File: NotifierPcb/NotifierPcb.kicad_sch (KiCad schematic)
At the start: 29 parts, among them IC1 CD4067BEE4, IC2 ESP32-WROOM-32E__8MB_, J1 RC_433_MHZ_RF, J2 UART_Conn, J3 Power_Conn, U1 HT75xx-1-SOT89

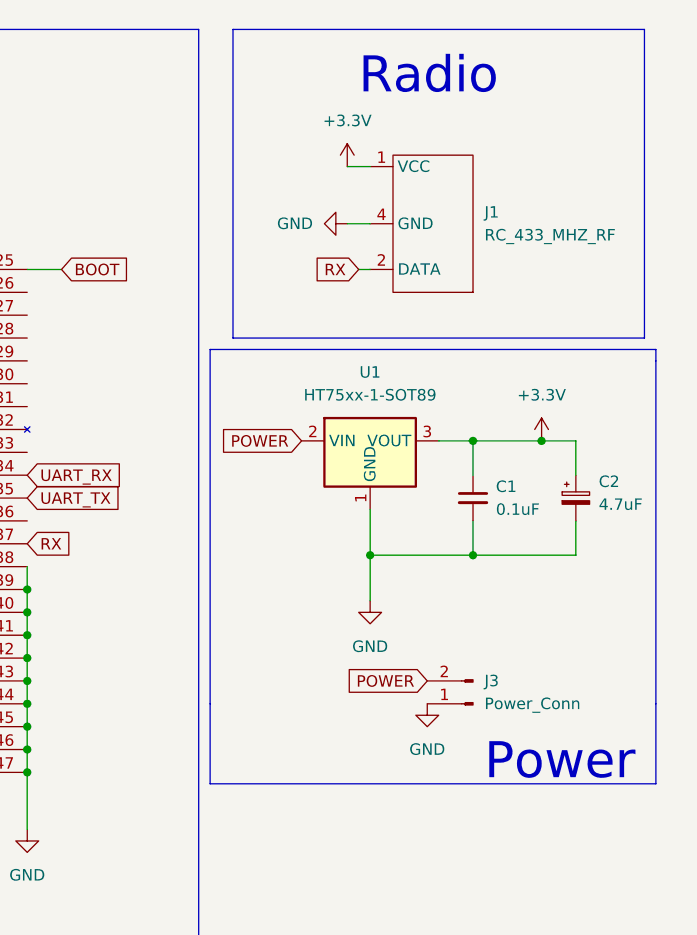
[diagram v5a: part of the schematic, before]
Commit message: power rf receiver with 5V
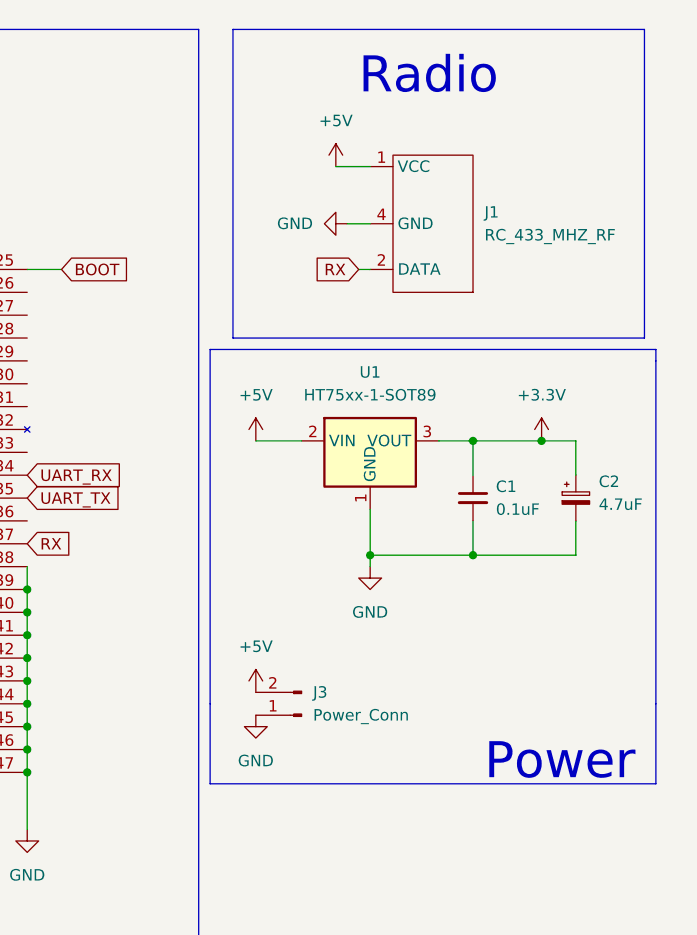
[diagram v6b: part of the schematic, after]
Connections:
- net +3.3V: no longer J1.1 (VCC)
- net POWER renamed +5V
- net +5V: now also J1.1 (VCC)
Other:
- moved on the sheet: J3
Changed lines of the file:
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@@
+    (stroke (width 0) (type default) (color 0 0 0 0))
+  )
+  (wire (pts (xy 238.76 64.77) (xy 243.84 64.77))
     (stroke (width 0) (type default) (color 0 0 0 0))
   )
@@
     (stroke (width 0) (type default) (color 0 0 0 0))
   )
-  (wire (pts (xy 248.92 34.29) (xy 251.46 34.29))
+  (wire (pts (xy 247.65 34.29) (xy 251.46 34.29))
     (stroke (width 0) (type default) (color 0 0 0 0))
   )
@@
     (stroke (width 0) (type default) (color 0 0 0 0))
   )
-  (wire (pts (xy 251.46 77.47) (xy 251.46 82.55))
+  (wire (pts (xy 251.46 77.47) (xy 251.46 78.74))
     (stroke (width 0) (type default) (color 0 0 0 0))
   )
@@
     )
   )
-  (global_label "POWER" (shape input) (at 257.81 91.44 180) (fields_autoplaced)
-    (effects (font (size 1.27 1.27)) (justify right))
-    (property "Intersheet References" "${INTERSHEET_REFS}" (id 0) (at 248.9259 91.3606 0)
-      (effects (font (size 1.27 1.27)) (justify right) hide)
-    )
-  )
   (global_label "BIT3" (shape input) (at 175.26 63.5 180) (fields_autoplaced)
     (effects (font (size 1.27 1.27)) (justify right))
@@
     (effects (font (size 1.27 1.27)) (justify right))
     (property "Intersheet References" "${INTERSHEET_REFS}" (id 0) (at 159.6631 138.5094 0)
-      (effects (font (size 1.27 1.27)) (justify right) hide)
-    )
-  )
-  (global_label "POWER" (shape input) (at 243.84 64.77 180) (fields_autoplaced)
-    (effects (font (size 1.27 1.27)) (justify right))
-    (property "Intersheet References" "${INTERSHEET_REFS}" (id 0) (at 234.9559 64.6906 0)
       (effects (font (size 1.27 1.27)) (justify right) hide)
     )
@@
     (pin "2")
     (pin "3")
+  )
+  (symbol (lib_id "power:+5V") (at 238.76 92.71 0) (unit 1)
+    (in_bom yes) (on_board yes) (fields_autoplaced)
+    (property "Reference" "#PWR?" (id 0) (at 238.76 96.52 0)
+      (effects (font (size 1.27 1.27)) hide)
+    )
+    (property "Value" "+5V" (id 1) (at 238.76 87.63 0))
+    (property "Footprint" "" (id 2) (at 238.76 92.71 0)
+      (effects (font (size 1.27 1.27)) hide)
+    )
+    (property "Datasheet" "" (id 3) (at 238.76 92.71 0)
+      (effects (font (size 1.27 1.27)) hide)
+    )
+    (pin "1")
   )
   (symbol (lib_id "Jumper:Jumper_2_Open") (at 199.39 151.13 0) (unit 1)
@@
     (pin "2")
   )
-  (symbol (lib_id "power:GND") (at 251.46 82.55 0) (unit 1)
-    (in_bom yes) (on_board yes) (fields_autoplaced)
-    (property "Reference" "#PWR011" (id 0) (at 251.46 88.9 0)
-      (effects (font (size 1.27 1.27)) hide)
-    )
-    (property "Value" "GND" (id 1) (at 251.46 87.63 0))
-    (property "Footprint" "" (id 2) (at 251.46 82.55 0)
-      (effects (font (size 1.27 1.27)) hide)
-    )
-    (property "Datasheet" "" (id 3) (at 251.46 82.55 0)
+  (symbol (lib_id "power:+5V") (at 247.65 34.29 0) (unit 1)
+    (in_bom yes) (on_board yes) (fields_autoplaced)
+    (property "Reference" "#PWR?" (id 0) (at 247.65 38.1 0)
+      (effects (font (size 1.27 1.27)) hide)
+    )
+    (property "Value" "+5V" (id 1) (at 247.65 29.21 0))
+    (property "Footprint" "" (id 2) (at 247.65 34.29 0)
+      (effects (font (size 1.27 1.27)) hide)
+    )
+    (property "Datasheet" "" (id 3) (at 247.65 34.29 0)
+      (effects (font (size 1.27 1.27)) hide)
+    )
+    (pin "1")
+  )
+  (symbol (lib_id "power:GND") (at 251.46 78.74 0) (unit 1)
+    (in_bom yes) (on_board yes) (fields_autoplaced)
+    (property "Reference" "#PWR011" (id 0) (at 251.46 85.09 0)
+      (effects (font (size 1.27 1.27)) hide)
+    )
+    (property "Value" "GND" (id 1) (at 251.46 83.82 0))
+    (property "Footprint" "" (id 2) (at 251.46 78.74 0)
+      (effects (font (size 1.27 1.27)) hide)
+    )
+    (property "Datasheet" "" (id 3) (at 251.46 78.74 0)
       (effects (font (size 1.27 1.27)) hide)
     )
@@
     )
     (property "Datasheet" "" (id 3) (at 170.18 143.51 0)
+      (effects (font (size 1.27 1.27)) hide)
+    )
+    (pin "1")
+  )
+  (symbol (lib_id "power:+5V") (at 238.76 64.77 0) (unit 1)
+    (in_bom yes) (on_board yes) (fields_autoplaced)
+    (property "Reference" "#PWR?" (id 0) (at 238.76 68.58 0)
+      (effects (font (size 1.27 1.27)) hide)
+    )
+    (property "Value" "+5V" (id 1) (at 238.76 59.69 0))
+    (property "Footprint" "" (id 2) (at 238.76 64.77 0)
+      (effects (font (size 1.27 1.27)) hide)
+    )
+    (property "Datasheet" "" (id 3) (at 238.76 64.77 0)
       (effects (font (size 1.27 1.27)) hide)
     )
@@
     (pin "2")
   )
-  (symbol (lib_id "power:+3.3V") (at 248.92 34.29 0) (unit 1)
-    (in_bom yes) (on_board yes) (fields_autoplaced)
-    (property "Reference" "#PWR03" (id 0) (at 248.92 38.1 0)
-      (effects (font (size 1.27 1.27)) hide)
-    )
-    (property "Value" "+3.3V" (id 1) (at 248.92 29.21 0))
-    (property "Footprint" "" (id 2) (at 248.92 34.29 0)
-      (effects (font (size 1.27 1.27)) hide)
-    )
-    (property "Datasheet" "" (id 3) (at 248.92 34.29 0)
-      (effects (font (size 1.27 1.27)) hide)
-    )
-    (pin "1")
-  )
-  (symbol (lib_id "power:GND") (at 257.81 93.98 0) (unit 1)
-    (in_bom yes) (on_board yes) (fields_autoplaced)
-    (property "Reference" "#PWR0101" (id 0) (at 257.81 100.33 0)
-      (effects (font (size 1.27 1.27)) hide)
-    )
-    (property "Value" "GND" (id 1) (at 257.81 99.06 0))
-    (property "Footprint" "" (id 2) (at 257.81 93.98 0)
-      (effects (font (size 1.27 1.27)) hide)
-    )
-    (property "Datasheet" "" (id 3) (at 257.81 93.98 0)
+  (symbol (lib_id "power:GND") (at 238.76 95.25 0) (unit 1)
+    (in_bom yes) (on_board yes) (fields_autoplaced)
+    (property "Reference" "#PWR0101" (id 0) (at 238.76 101.6 0)
+      (effects (font (size 1.27 1.27)) hide)
+    )
+    (property "Value" "GND" (id 1) (at 238.76 100.33 0))
+    (property "Footprint" "" (id 2) (at 238.76 95.25 0)
+      (effects (font (size 1.27 1.27)) hide)
+    )
+    (property "Datasheet" "" (id 3) (at 238.76 95.25 0)
       (effects (font (size 1.27 1.27)) hide)
     )
@@
     (pin "1")
   )
-  (symbol (lib_id "Connector:Conn_01x02_Male") (at 262.89 93.98 180) (unit 1)
-    (in_bom yes) (on_board yes) (fields_autoplaced)
-    (property "Reference" "J3" (id 0) (at 264.16 91.4399 0)
+  (symbol (lib_id "Connector:Conn_01x02_Male") (at 243.84 95.25 180) (unit 1)
+    (in_bom yes) (on_board yes) (fields_autoplaced)
+    (property "Reference" "J3" (id 0) (at 245.11 92.7099 0)
       (effects (font (size 1.27 1.27)) (justify right))
     )
-    (property "Value" "Power_Conn" (id 1) (at 264.16 93.9799 0)
+    (property "Value" "Power_Conn" (id 1) (at 245.11 95.2499 0)
       (effects (font (size 1.27 1.27)) (justify right))
     )
-    (property "Footprint" "Connector_PinHeader_2.54mm:PinHeader_1x02_P2.54mm_Vertical" (id 2) (at 262.89 93.98 0)
-      (effects (font (size 1.27 1.27)) hide)
-    )
-    (property "Datasheet" "~" (id 3) (at 262.89 93.98 0)
+    (property "Footprint" "Connector_PinHeader_2.54mm:PinHeader_1x02_P2.54mm_Vertical" (id 2) (at 243.84 95.25 0)
+      (effects (font (size 1.27 1.27)) hide)
+    )
+    (property "Datasheet" "~" (id 3) (at 243.84 95.25 0)
       (effects (font (size 1.27 1.27)) hide)
     )
@@
       (reference "#PWR01") (unit 1) (value "+3.3V") (footprint "")
     )
-    (path "/ba17a5d4-03e3-4f0c-8953-4fd95bbdcc72"
-      (reference "#PWR03") (unit 1) (value "+3.3V") (footprint "")
-    )
     (path "/ee4b48cc-ac4a-4c5a-9b29-8707b5eac42b"
       (reference "#PWR04") (unit 1) (value "GND") (footprint "")
@@
       (reference "#PWR0105") (unit 1) (value "VCC") (footprint "")
     )
+    (path "/0b94bdc1-1b31-4a34-b7eb-38beeb2cd809"
+      (reference "#PWR?") (unit 1) (value "+5V") (footprint "")
+    )
+    (path "/8e76776a-e489-41d1-8d03-c5ea4043c05f"
+      (reference "#PWR?") (unit 1) (value "+5V") (footprint "")
+    )
+    (path "/9cb21bed-a369-40ff-a71a-a1ce36f197f0"
+      (reference "#PWR?") (unit 1) (value "+5V") (footprint "")
+    )
     (path "/36e34b7d-0786-44b4-832b-9944d0f666aa"
